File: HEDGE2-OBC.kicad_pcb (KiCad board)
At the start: 4 copper layers, 90.2 x 95.9 mm, 59 parts, among them J1 MMBX-S50-0-18, J2 SQT-110-01-L-D, J3 SMA-J-P-X-RA-TH1, U1 ADP7158ARDZ-3.3-R7, U2 INA260AIPWR, U3 INA260AIPWR, U4 SN65HVD1782QDRQ1, U5 SN65HVD1782QDRQ1, U6 TCAN1046AVDYYRQ1

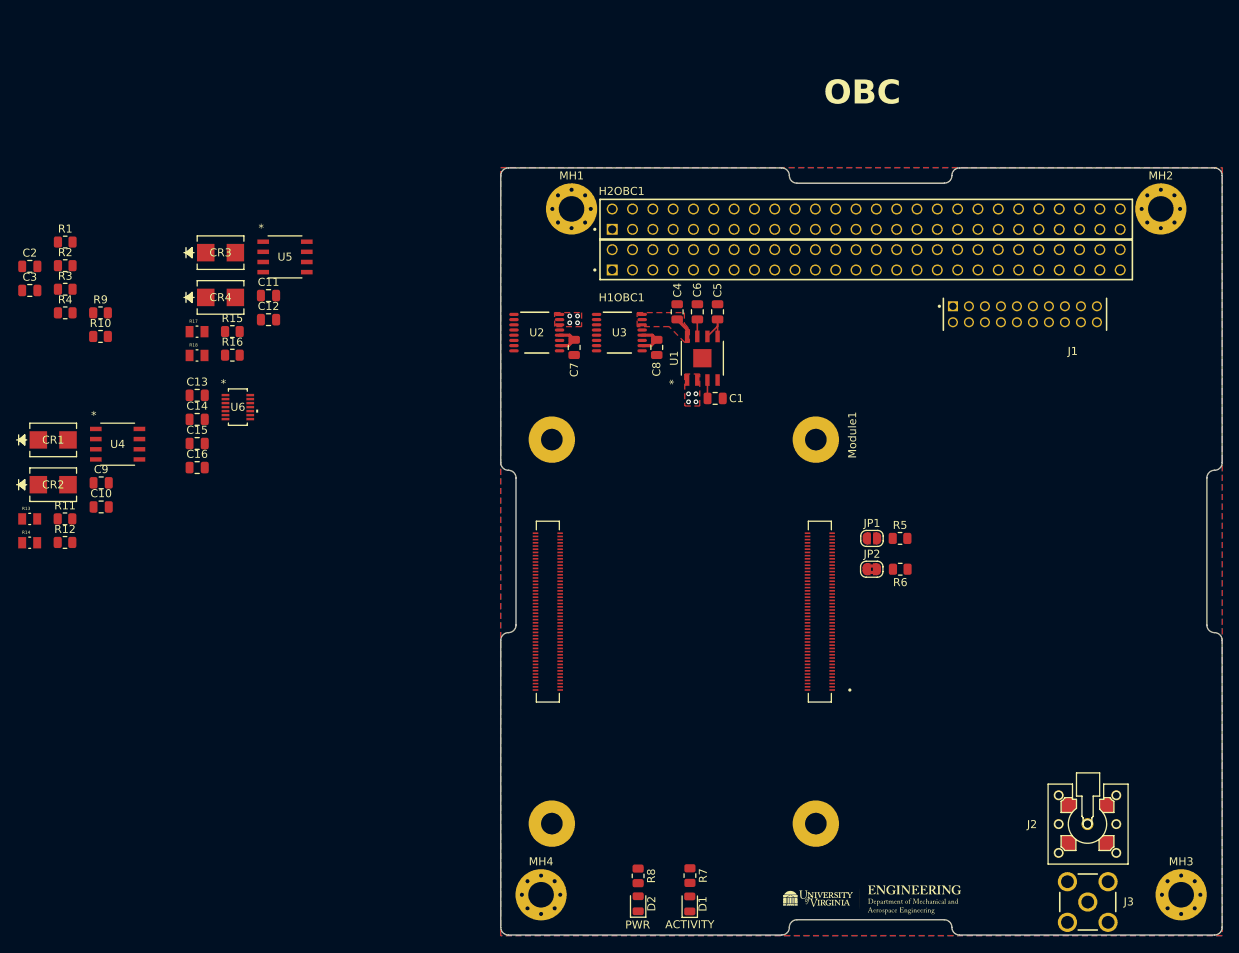
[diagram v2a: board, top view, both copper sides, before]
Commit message: Rework Novatel OEM719B symbol and footprint
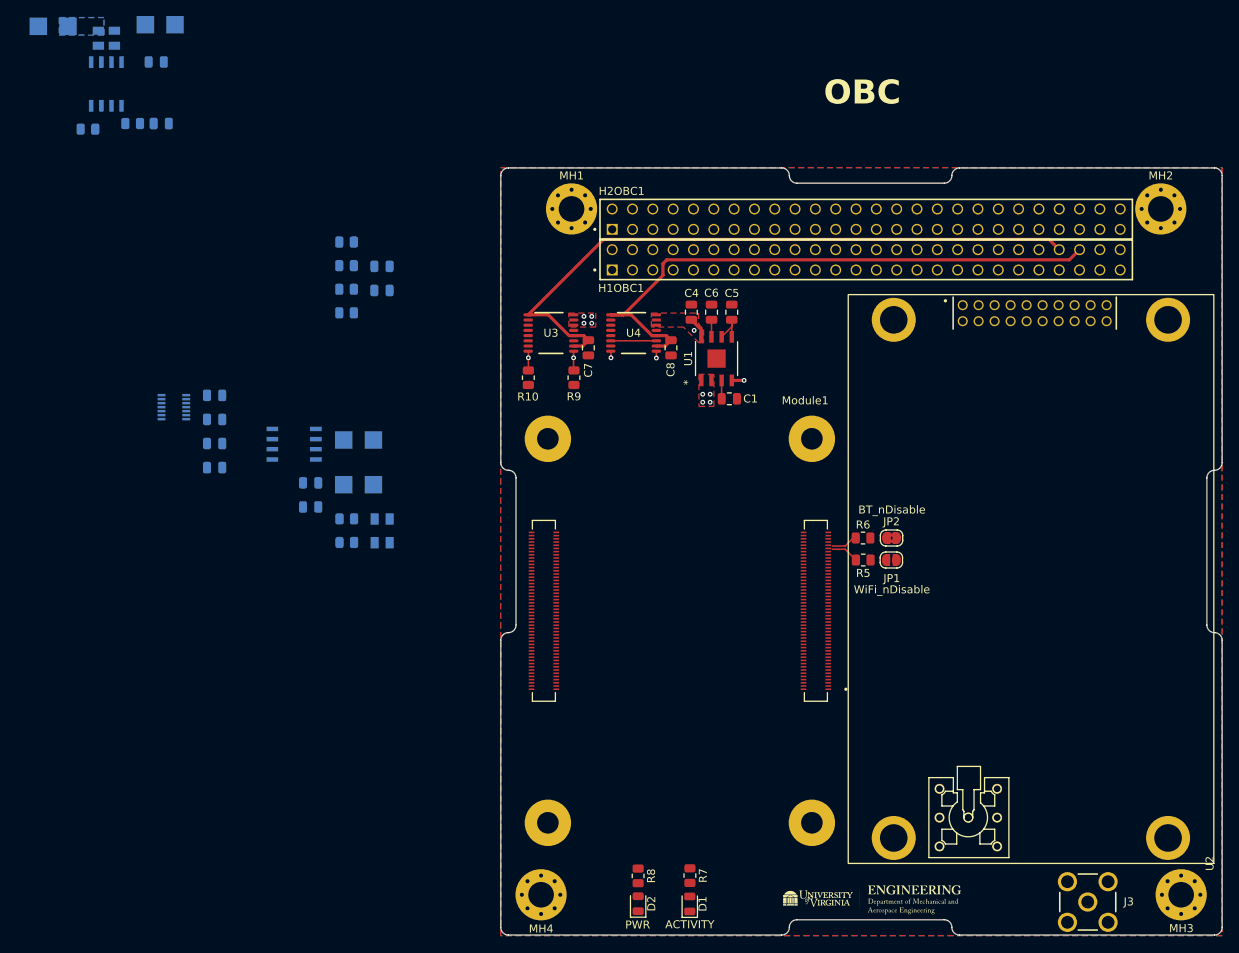
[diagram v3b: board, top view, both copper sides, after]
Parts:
- removed J1: MMBX-S50-0-18, SQT-110-01-L-D:SAMTEC_SQT-110-01-L-D
- removed J2: SQT-110-01-L-D, Novatel:MMBX-S50-0-18
- added U2: ~, OEM719B:OEM719B, F.Cu at (253.2, 176.5)
- C10, C11, C12, C13, C14, C15, C16, C2, C3, C9, CR1, CR2, CR3, CR4, R1, R11, R12, R13, R14, R15, R16, R17, R18, R2, R3, R4: moved to B.Cu
- U5: renamed from U4; moved to B.Cu
- U6: renamed from U5; moved to B.Cu
- U7: renamed from U6; moved to B.Cu
- moved R9 59.7 mm to (173.2, 115.8), turned to -90 degrees
- moved R10 53.7 mm to (167.6, 115.8), turned to -90 degrees
- moved R13 44.1 mm to (149.3, 133.4), turned to 180 degrees
- moved R14 44.1 mm to (149.3, 136.4), turned to 180 degrees
- moved C2 44.0 mm to (149.3, 101.8), turned to 180 degrees
- moved C3 44.0 mm to (149.3, 104.9), turned to 180 degrees
- moved R18 41.5 mm to (113.8, 73.3), turned to 90 degrees
- moved CR4 39.8 mm to (108.2, 71.8)
- moved CR1 38.2 mm to (146.3, 123.5), turned to 180 degrees
- moved CR2 38.2 mm to (146.3, 129.1), turned to 180 degrees
- moved R17 38.1 mm to (115.8, 73.3), turned to 90 degrees
- moved R11 35.2 mm to (144.9, 133.4), turned to 180 degrees
- moved R12 35.2 mm to (144.9, 136.4), turned to 180 degrees
- moved R1 35.2 mm to (144.8, 98.8), turned to 180 degrees
- moved R2 35.2 mm to (144.8, 101.8), turned to 180 degrees
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- renumbered U2 to U3, U3 to U4
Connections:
- J3 pad 1: /RF_GNSS -> Net-(U2-ANT)
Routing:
- net +5V_MPU: track 4.19 -> 81.8 mm
- net +5V_GNSS: track 4.19 -> 73.8 mm
- net /SCL0: track 0.00 -> 14.1 mm, vias 0 -> 2
- net /SDA0: track 0.00 -> 14.1 mm, vias 0 -> 2
- net +5V_OEM719B: track 2.64 -> 13.0 mm, vias 0 -> 2
- net GND: track 0.00 -> 5.70 mm
- net Net-(Module1A-WiFi_nDisable): track 0.00 -> 3.53 mm
- net Net-(Module1A-BT_nDisable): track 0.00 -> 3.36 mm
- added copper zone on In1.Cu, net +5V_GNSS
- added copper zone on In1.Cu, net +5V_MPU
- added copper zone on B.Cu, net /UART_D_RX

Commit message: Layout PCB; update footprints with 3D models
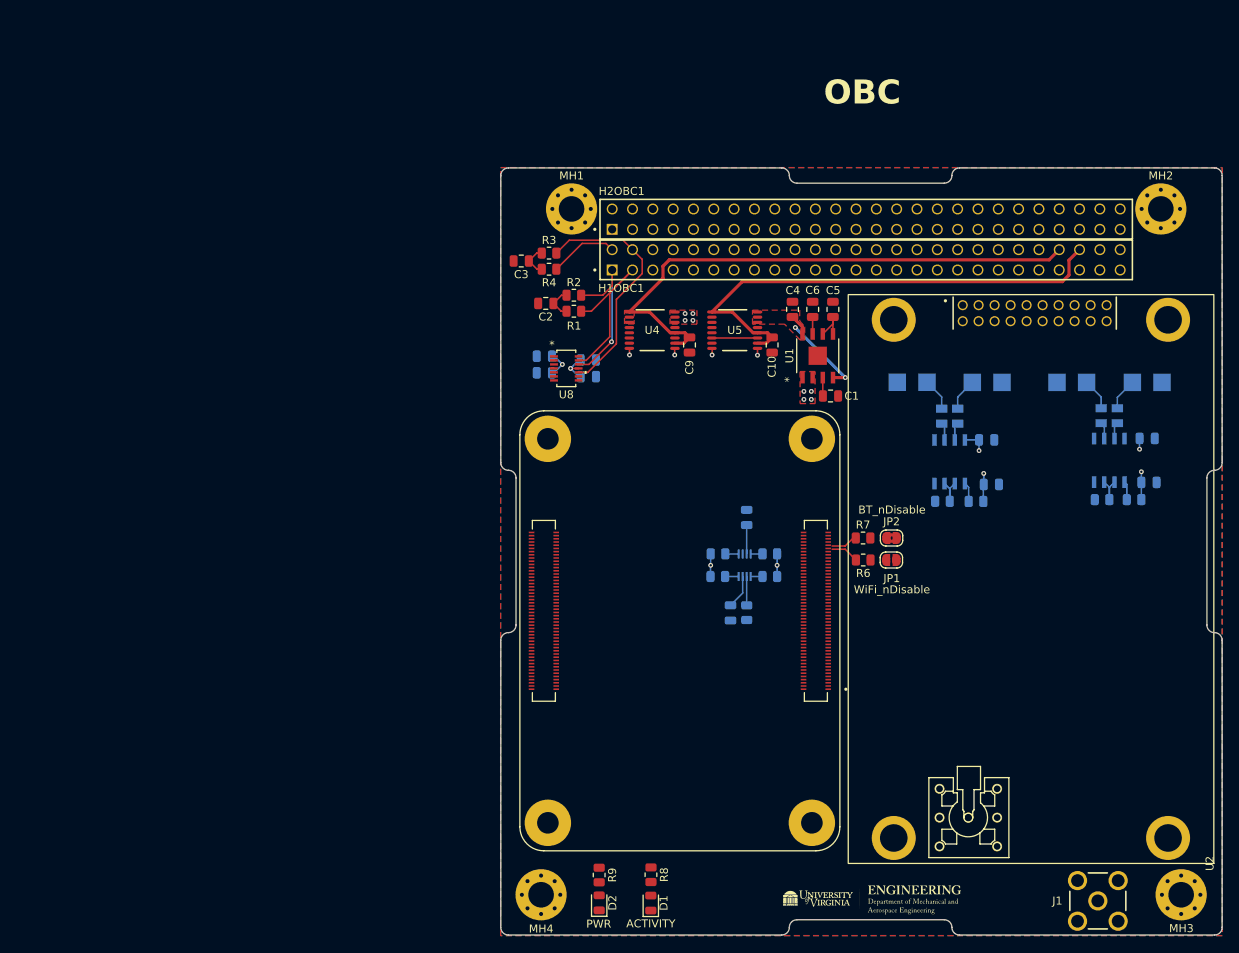
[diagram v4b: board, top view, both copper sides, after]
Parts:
- removed J3: SMA-J-P-X-RA-TH1, SMA_J_P_H_RA_TH1:SAMTEC_SMA-J-P-X-RA-TH1
- added C7: 0u1, Capacitor_SMD:C_0805_2012Metric, B.Cu at (194.8, 133.2)
- added C8: 0u1, Capacitor_SMD:C_0805_2012Metric, B.Cu at (192.8, 145.2)
- added J1: SMA-J-P-X-RA-TH1, SMA_J_P_H_RA_TH1:SAMTEC_SMA-J-P-X-RA-TH1, F.Cu at (238.7, 181.2)
- added R20: 4k7, Resistor_SMD:R_0805_2012Metric, B.Cu at (191.3, 137.8)
- added R21: 4k7, Resistor_SMD:R_0805_2012Metric, B.Cu at (191.2, 140.6)
- added R5: 10k, Resistor_SMD:R_0805_2012Metric, B.Cu at (194.8, 145.1)
- added U3: TXS0102QDCURQ1, TXS0102QDCURQ1:SOP50P310X90-8N, B.Cu at (194.6, 139.2)
- C2, C3, R1, R2, R3, R4: moved to F.Cu
- R10: renamed from R9; moved to B.Cu
- R11: renamed from R10; moved to B.Cu
- U8: renamed from U7; moved to F.Cu
- moved R17 116.5 mm to (219.3, 131.2)
- moved CR4 116.2 mm to (215.5, 116.3)
- moved R16 115.5 mm to (223.5, 131.2)
- moved R18 115.5 mm to (221.2, 120.6)
- moved R19 115.5 mm to (219.2, 120.6)
- moved U7 115.5 mm to (220.2, 126.3)
- moved C13 114.1 mm to (224.8, 123.5)
- moved C14 113.1 mm to (225.4, 129.1)
- moved CR3 112.6 mm to (224.9, 116.3)
- moved C12 104.8 mm to (245.1, 128.8)
- moved C11 104.7 mm to (244.9, 123.3)
- moved U6 101.9 mm to (240.2, 126.1), turned to 90 degrees
- moved CR1 98.8 mm to (244.9, 116.3)
- moved R12 98.4 mm to (243.3, 131.0)
- moved R13 94.6 mm to (239.3, 131.0)
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- renumbered C8 to C10, C9 to C11, C10 to C12, C11 to C13, C12 to C14, C13 to C15, C14 to C16, C15 to C17, C16 to C18, C7 to C9, R11 to R12, R12 to R13, R13 to R14, R14 to R15, R15 to R16, R16 to R17, R17 to R18, R18 to R19, R5 to R6, R6 to R7, R7 to R8, R8 to R9, U3 to U4, U4 to U5, U5 to U6, U6 to U7
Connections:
- Module1 pad 80: /SCL0 -> /SCL0_3V3
- Module1 pad 82: /SDA0 -> /SDA0_3V3
- R10 pad 1: /SCL0 -> /SCL0_3V3
- R11 pad 1: /SDA0 -> /SDA0_3V3
- U4 pad 8: /SDA0 -> /SDA0_5V
- U4 pad 9: /SCL0 -> /SCL0_5V
- U5 pad 8: /SDA0 -> /SDA0_5V
- U5 pad 9: /SCL0 -> /SCL0_5V
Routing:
- net /CAN_B_H: track 0.00 -> 30.5 mm
- net /CAN_A_H: track 0.00 -> 23.2 mm
- net /CAN_A_L: track 0.00 -> 20.6 mm, vias 0 -> 1
- net +5V_CM4: track 0.00 -> 15.9 mm, vias 4 -> 9
- net /SCL0: track 14.1 -> 0.00 mm, vias 2 -> 0
- net /SDA0: track 14.1 -> 0.00 mm, vias 2 -> 0
- net +5V_GNSS: track 73.8 -> 61.2 mm
- net /GNSS_RXD1: track 0.00 -> 10.9 mm
- net +3V3: track 0.00 -> 9.90 mm, vias 0 -> 2
- net /CAN_B_L: track 0.00 -> 8.64 mm
- net /GNSS_TXD1: track 0.00 -> 8.18 mm
- net +5V_MPU: track 81.8 -> 75.9 mm, vias 0 -> 1
- net /UART_COMM_DIR: track 0.00 -> 4.95 mm
- net /UART_SCI_DIR: track 0.00 -> 4.88 mm
- net /UART_SCI_B: track 0.00 -> 4.71 mm
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- added copper zone on F.Cu, net +5V_MPU
- removed copper zone on B.Cu, net /UART_D_RX

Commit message: Continue PCB layout
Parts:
- moved C7 0.91 mm to (194.9, 132.3)
- moved C8 0.91 mm to (192.8, 144.2)
- moved R10 0.91 mm to (197.8, 139.7)
- moved R11 0.91 mm to (197.8, 136.9)
- moved R20 0.91 mm to (191.3, 136.9)
- moved R21 0.91 mm to (191.3, 139.7)
- moved R5 0.91 mm to (194.9, 144.2)
- moved U3 0.91 mm to (194.6, 138.3)
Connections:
- Module1 pad 26: unconnected-(Module1A-GPIO19-Pad26) -> /UART_SCI_DIR
- Module1 pad 29: /CAN_A_S -> unconnected-(Module1A-GPIO16-Pad29)
- Module1 pad 30: unconnected-(Module1A-GPIO6-Pad30) -> /I2C_EN
- Module1 pad 37: unconnected-(Module1A-GPIO7-Pad37) -> /CAN_B_S
- Module1 pad 38: /GNSS_NRESET_IN -> unconnected-(Module1A-GPIO11-Pad38)
- Module1 pad 39: /UART_SCI_A -> /UART_COMM_A
- Module1 pad 40: /UART_SCI_B -> /UART_COMM_B
- Module1 pad 41: unconnected-(Module1A-GPIO25-Pad41) -> /UART_COMM_DIR
- Module1 pad 45: /UART_SCI_DIR -> unconnected-(Module1A-GPIO24-Pad45)
- Module1 pad 47: /UART_COMM_DIR -> unconnected-(Module1A-GPIO23-Pad47)
- Module1 pad 48: unconnected-(Module1A-GPIO27-Pad48) -> /GNSS_NRESET_IN
- Module1 pad 49: unconnected-(Module1A-GPIO18-Pad49) -> /CAN_A_S
- Module1 pad 58: /CAN_B_S -> unconnected-(Module1A-GPIO2-Pad58)
- R16 pad 2: /UART_SCI_B -> /UART_COMM_B
- U7 pad 1: /UART_SCI_B -> /UART_COMM_B
- U7 pad 4: /UART_SCI_A -> /UART_COMM_A
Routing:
- net /nPWR_LED: track 0.00 -> 70.8 mm, vias 0 -> 2
- net /PI_nLED_Activity: track 0.00 -> 48.4 mm
- net /UART_SCI_A: track 0.00 -> 43.6 mm, vias 0 -> 1
- net /UART_SCI_B: track 4.71 -> 44.9 mm, vias 0 -> 1
- net /UART_SCI_DIR: track 4.88 -> 44.9 mm, vias 0 -> 1
- net /SCL0_5V: track 3.37 -> 42.3 mm
- net /SDA0_5V: track 3.37 -> 41.7 mm
- net Net-(U2-ANT): track 0.00 -> 20.5 mm
- net /SDA0_3V3: track 1.48 -> 9.67 mm, vias 0 -> 1
- net GND: track 5.70 -> 13.9 mm
- net /SCL0_3V3: track 1.48 -> 9.15 mm, vias 0 -> 1
- net +3V3: track 9.90 -> 17.4 mm
- net /UART_COMM_B: track 0.00 -> 2.42 mm
- net Net-(Module1A-WiFi_nDisable): track 3.53 -> 4.07 mm
- net +5V_CM4: track 15.9 -> 16.3 mm, vias 9 -> 12
- removed copper zone on In1.Cu, net +5V_GNSS
- removed copper zone on In1.Cu, net +5V_MPU
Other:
- board text added: "HEDGE-2 OBC V1.1"

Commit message: Continue layout
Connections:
- C8 pad 1: +5V_MPU -> +5V_CM4
- R20 pad 2: +5V_MPU -> +5V_CM4
- R21 pad 2: +5V_MPU -> +5V_CM4
- U3 pad 7: +5V_MPU -> +5V_CM4
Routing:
- net /CAN_A_RXD: track 0.00 -> 53.4 mm, vias 0 -> 2
- net /CAN_B_S: track 0.00 -> 52.0 mm
- net /CAN_A_S: track 0.00 -> 51.7 mm, vias 0 -> 2
- net /CAN_A_TXD: track 0.00 -> 50.0 mm, vias 0 -> 2
- net /CAN_B_RXD: track 0.00 -> 49.6 mm, vias 0 -> 2
- net /CAN_B_TXD: track 0.00 -> 46.0 mm
- net /UART_E_TX: track 4.01 -> 42.1 mm
- net /UART_E_RX: track 3.99 -> 39.3 mm
- net /UART_D_TX: track 4.03 -> 35.3 mm
- net /UART_COMM_B: track 2.42 -> 31.4 mm, vias 0 -> 3
- net /UART_COMM_A: track 0.00 -> 27.0 mm, vias 0 -> 2
- net /UART_D_RX: track 4.06 -> 28.7 mm
- net /UART_COMM_DIR: track 4.95 -> 29.2 mm, vias 0 -> 1
- net +3V3_OEM719B: track 0.00 -> 22.6 mm
- net /CAN_B_L: track 8.64 -> 25.3 mm, vias 0 -> 2
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- added copper zone on F.Cu, net +3V3
- added copper zone on In1.Cu, net +3V3
- removed copper zone on In1.Cu, net +3V3_OEM719B

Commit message: ERC/DRC
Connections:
- Module1 pad SH1: (no net) -> GND
- Module1 pad SH2: (no net) -> GND
- Module1 pad SH3: (no net) -> GND
- Module1 pad SH4: (no net) -> GND
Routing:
- net /GNSS_PPS: track 0.00 -> 76.5 mm, vias 0 -> 1
- net /GNSS_RXD2: track 0.00 -> 67.4 mm, vias 0 -> 1
- net GND: track 19.0 -> 40.9 mm, vias 2 -> 13
- net /5V_PERM: track 0.00 -> 7.62 mm
- net /BATT: track 0.00 -> 2.54 mm
- net /CAN_B_RXD: track 49.6 -> 51.4 mm
- net Net-(D1-A): track 0.00 -> 1.70 mm
- net Net-(D2-A): track 0.00 -> 1.63 mm
- net +5V_CM4: track 27.8 -> 26.5 mm
- net /CAN_A_L: track 20.6 -> 19.5 mm
- net +5V_MPU: track 72.4 -> 71.3 mm, vias 1 -> 0
- net /CAN_A_RXD: track 53.4 -> 54.3 mm
- net /CAN_B_L: track 25.3 -> 24.8 mm
- net /SCL0_5V: vias 2 -> 1
- net +3V3_OEM719B: vias 4 -> 1
- added copper zone on B.Cu, net +5V_CM4
- added copper zone on F.Cu, net +5V_GNSS

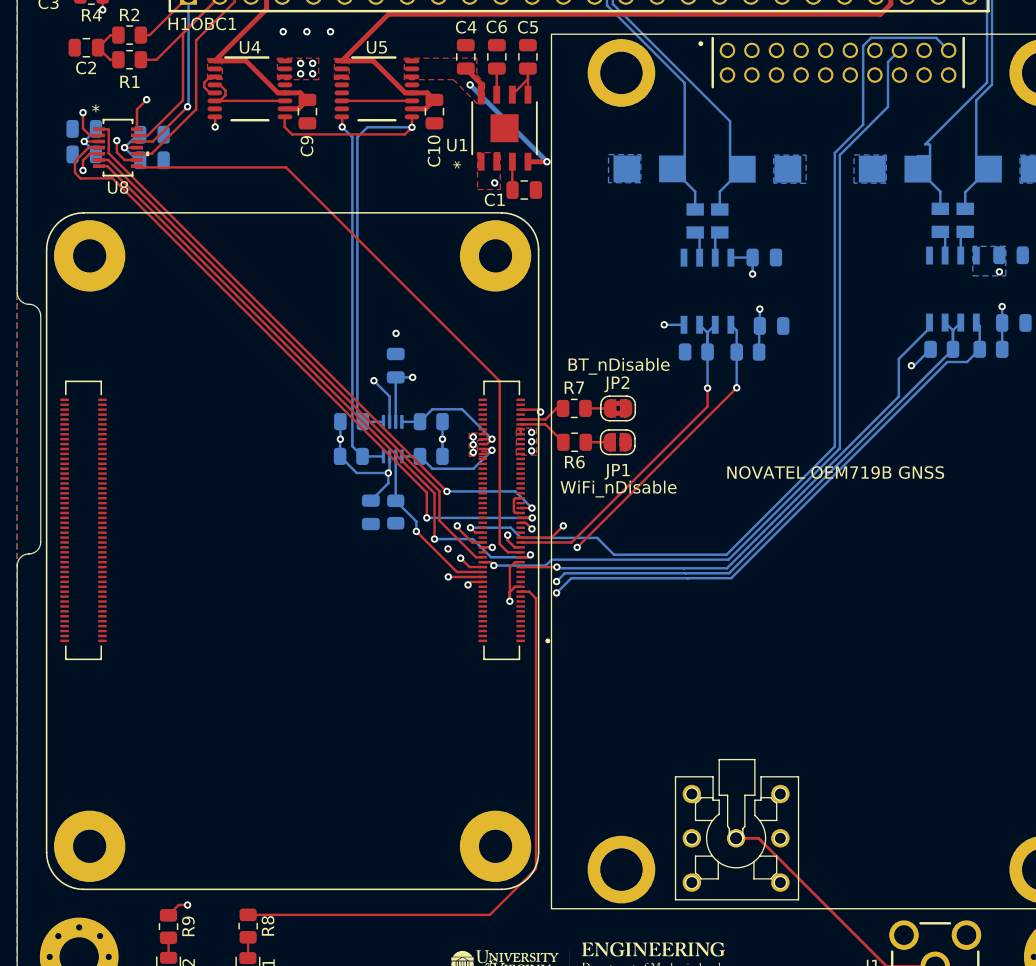
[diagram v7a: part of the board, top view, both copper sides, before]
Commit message: Fix MMBX footprint; resolve ERC/DRC
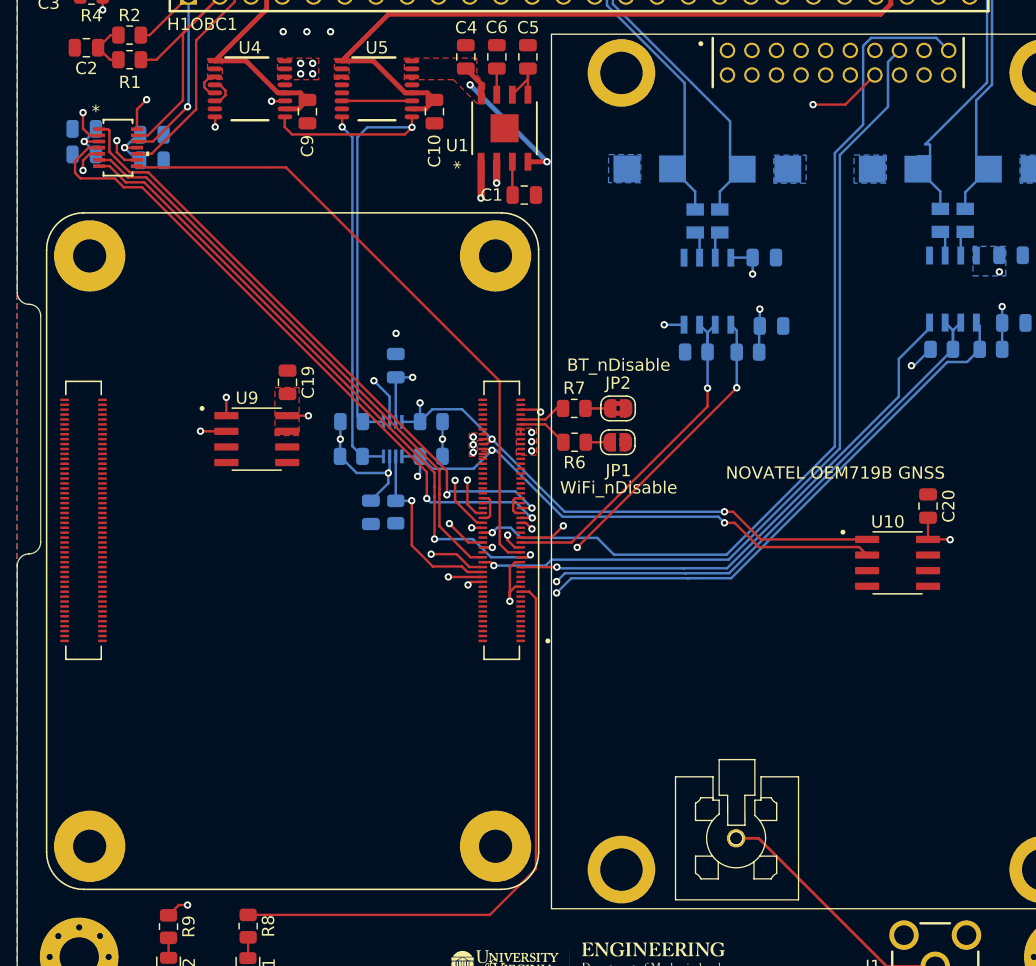
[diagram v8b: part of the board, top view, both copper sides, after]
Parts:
- added C19: 0u1, Capacitor_SMD:C_0805_2012Metric, F.Cu at (186.1, 133.7)
- added C20: 0u1, Capacitor_SMD:C_0805_2012Metric, F.Cu at (238.2, 143.7)
- added U10: MAX6633MSA_T, MAX6635MSA_T:SOIC127P600X175-8N, F.Cu at (235.7, 148.4)
- added U9: MAX6633MSA_T, MAX6635MSA_T:SOIC127P600X175-8N, F.Cu at (183.6, 138.3)
- moved C1 0.41 mm to (205.3, 118.5)
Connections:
- Module1 pad SH1: GND -> (no net)
- Module1 pad SH2: GND -> (no net)
- Module1 pad SH3: GND -> (no net)
- Module1 pad SH4: GND -> (no net)
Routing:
- net /GNSS_PV: track 0.00 -> 59.9 mm, vias 0 -> 1
- net /SCL0_3V3: track 9.15 -> 68.4 mm, vias 1 -> 4
- net /SDA0_3V3: track 9.67 -> 62.5 mm, vias 1 -> 4
- net /GNSS_TXD2: track 0.00 -> 52.3 mm, vias 0 -> 2
- net /GNSS_NRESET_IN: track 0.00 -> 51.4 mm, vias 0 -> 1
- net +3V3_OEM719B: track 22.6 -> 52.4 mm, vias 1 -> 2
- net +3V3: track 11.9 -> 17.2 mm, vias 6 -> 8
- net /GNSS_PPS: track 76.5 -> 74.5 mm
- net /I2C_EN: track 13.6 -> 15.2 mm
- net /CAN_A_TXD: track 50.0 -> 51.3 mm
- net /CAN_B_TXD: track 46.0 -> 47.2 mm
- net GND: track 40.9 -> 42.2 mm
- net /CAN_B_RXD: track 51.4 -> 52.4 mm
- removed copper zone on F.Cu, net +3V3_OEM719B
